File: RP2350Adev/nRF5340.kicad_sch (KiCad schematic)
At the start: 1 part, among them U1 NRF5340-CLAA-R

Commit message: Updated nRF5340 work
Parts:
- removed U1: NRF5340-CLAA-R, WLCSP95_4.390X3.994_NOR, symbol nRF5340:NRF5340-CLAA-R
- added C1, C7, C9: 1.0uF, symbol Device:C
- added C10: 2.2nF, symbol Device:C
- added C11: 2.2uF, symbol Device:C
- added C2, C3: 0.7pF, symbol Device:C
- added C4, C5, C8: 4.7uF, symbol Device:C
- added C6: 100nnF, symbol Device:C
- added L1, L3, L4: 10uH, symbol Device:L
- added L2: 2.2nH, symbol Device:L
- added R1: R, symbol Device:R
- added U1: nRF5340-QKxx, Package_DFN_QFN:Nordic_AQFN-94-1EP_7x7mm_P0.4mm, symbol MCU_Nordic:nRF5340-QKxx
- added X1: 32MHz, symbol Device:Crystal
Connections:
- new net: C10.1, C9.1, L4.2, U1.A27 (DECR), U1.G31 (DECRF)
- new net: C3.1, L2.2, U1.L31 (ANT)
- new net: C2.1, L2.1
- new net: U1.B30 (XC2), X1.1
- new net: U1.C31 (XC1), X1.2
- new net: C7.1, U1.A13 (DECA)
- new net: C1.1, L1.2, U1.A15 (DECD)
- new net: L4.1, U1.A21 (DCC)
- new net: C6.1, U1.A23 (DECN)
- new net: C4.1, R1.2, U1.A5 (VBUS)
- new net: L1.1, U1.B10 (DCCD)
- new net: C5.1, U1.B6 (DECUSB)
- new net: L3.2, U1.J1 (DCCH)
- new net VDD_HV: C8.2, U1.E1 (VDDH)
- new net VDD_nRF: C11.2, L3.1, U1.A19 (VDD), U1.AC1 (VDD), U1.AG1 (VDD), U1.AJ31 (VDD), U1.AL11 (VDD), U1.AL17 (VDD), U1.AL25 (VDD), U1.AL3 (VDD), U1.AL7 (VDD), U1.B28 (VDD), U1.B8 (VDD), U1.C1 (VDD), U1.E31 (VDD), U1.L1 (VDD), U1.N31 (VDD), U1.U1 (VDD)

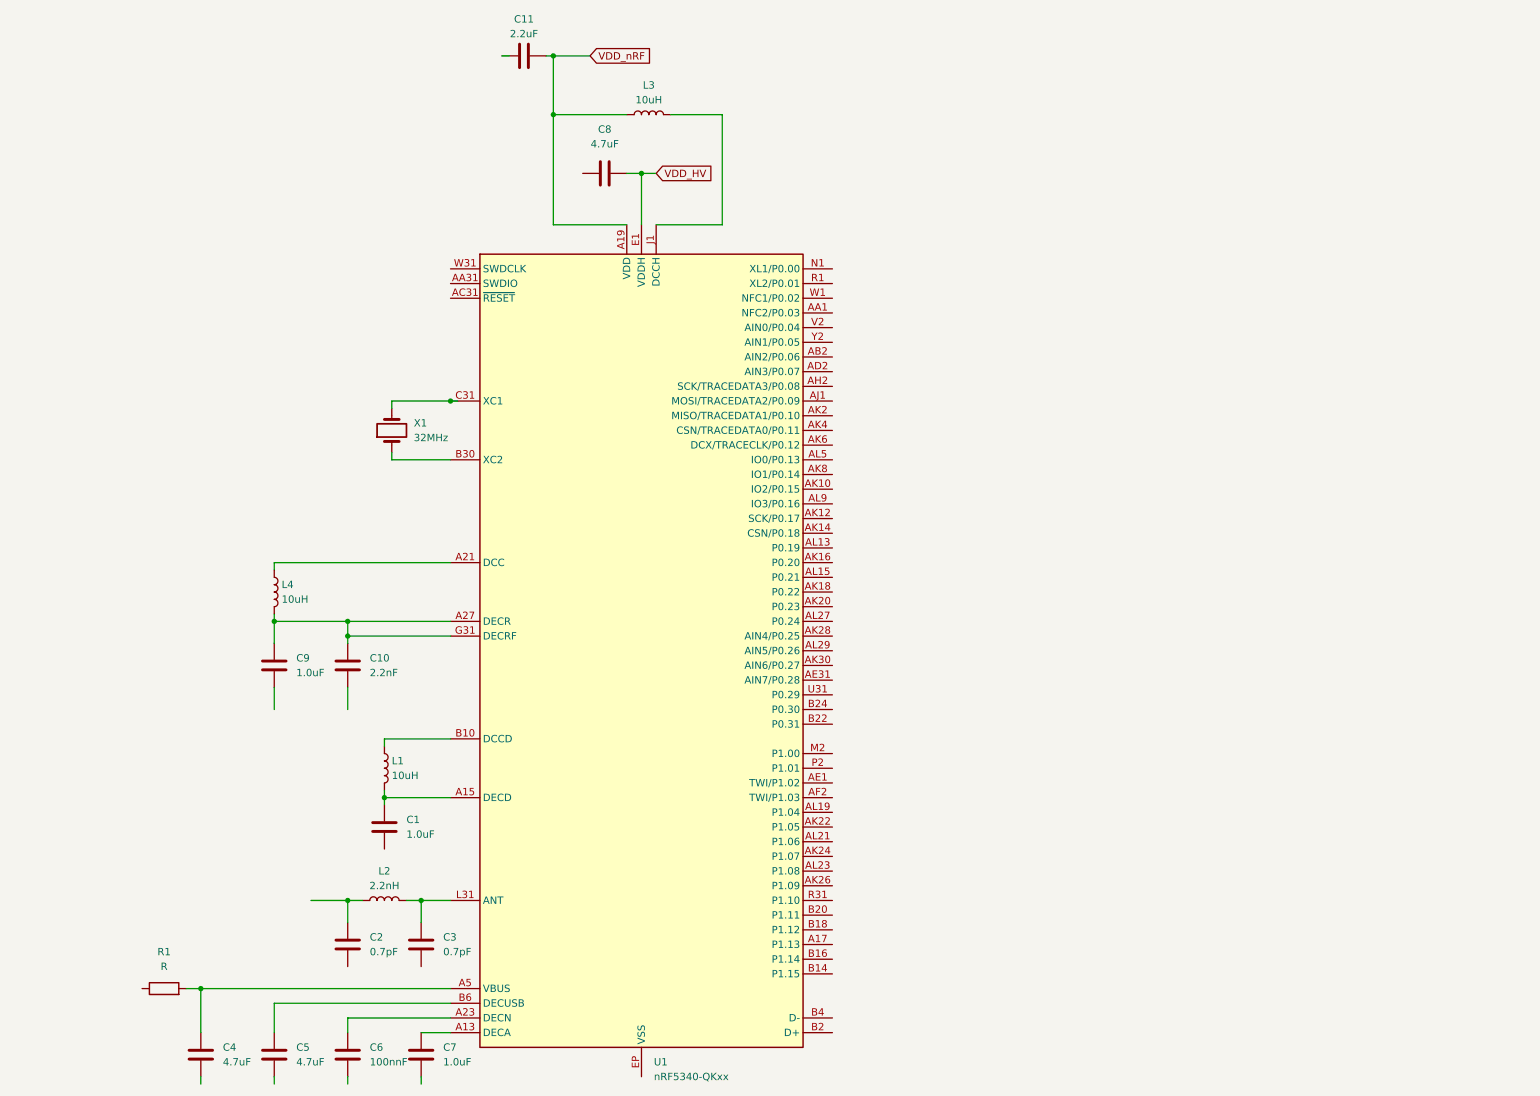
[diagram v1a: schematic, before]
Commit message: Updated nRF5340 schematic
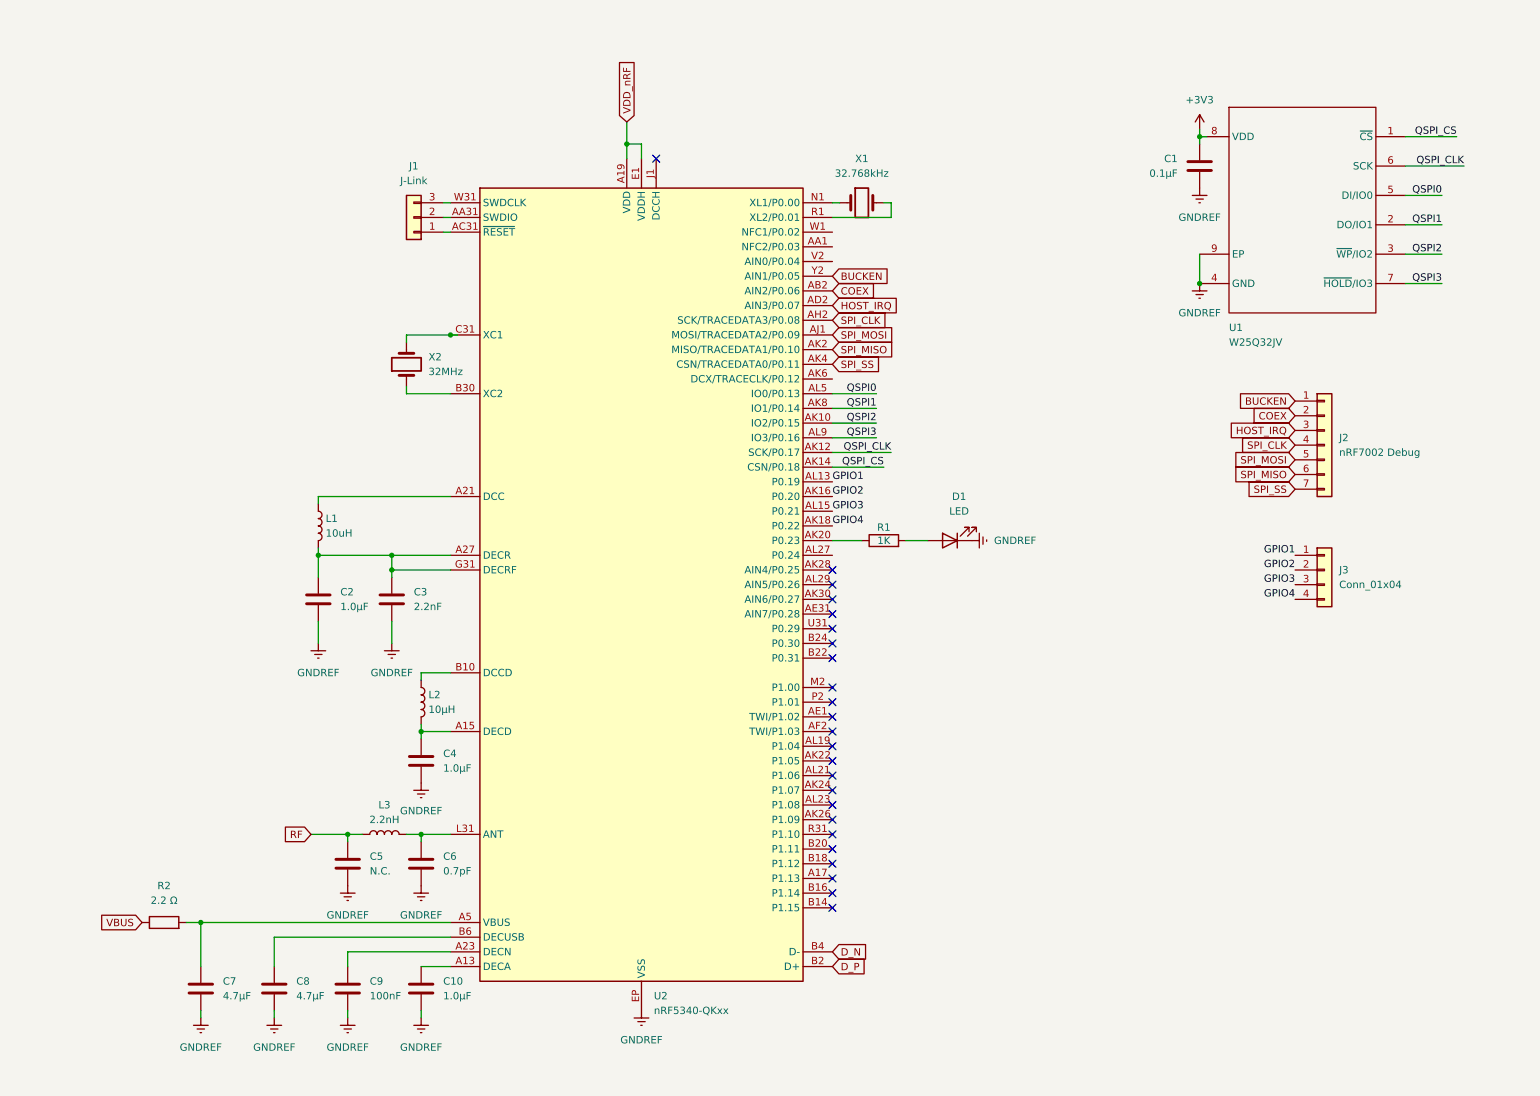
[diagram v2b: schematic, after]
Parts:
- removed C11: 2.2uF, symbol Device:C
- removed C8: 4.7uF, symbol Device:C
- removed L3: 10uH, symbol Device:L
- added C1: 0.1µF, Resistor_SMD:R_0402_1005Metric, symbol Device:C
- added D1: LED, symbol Device:LED
- added J1: J-Link, symbol Connector_Generic:Conn_01x03
- added J2: nRF7002 Debug, symbol Connector_Generic:Conn_01x07
- added J3: Conn_01x04, symbol Connector_Generic:Conn_01x04
- added R1: 1K, Resistor_SMD:R_0402_1005Metric, symbol Device:R
- added U1: W25Q32JV, Package_SON:WSON-8-1EP_6x5mm_P1.27mm_EP3.4x4.3mm, symbol Eclectronics:W25Q128JV
- added X1: 32.768kHz, symbol Device:Crystal
- C10: renamed from C7; value 1.0uF -> 1.0µF
- C2: renamed from C9; value 1.0uF -> 1.0µF
- C4: renamed from C1; value 1.0uF -> 1.0µF
- C5: renamed from C2; value 0.7pF -> N.C.
- C7: renamed from C4; value 4.7uF -> 4.7µF
- C8: renamed from C5; value 4.7uF -> 4.7µF
- C9: renamed from C6; value 100nnF -> 100nF
- L2: renamed from L1; value 10uH -> 10µH
- R2: renamed from R1; value R -> 2.2 Ω
- renumbered C10 to C3, C3 to C6, L4 to L1, L2 to L3, U1 to U2, X1 to X2
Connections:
- net VDD_HV is gone; now on net VDD_nRF: U2.E1 (VDDH)
- net GNDREF: now reaches C2.2
- net GNDREF: now also C10.2, C3.2, C4.2, C5.2, C6.2, C7.2, C8.2, C9.2, U2.EP (VSS), C1.1, D1.1 (K), U1.4 (GND), U1.9 (EP)
- net RF: now reaches C5.1, L3.1
- net at U2.AA31 (SWDIO): now also J1.2 (Pin_2)
- net COEX: now reaches U2.AB2 (AIN2/P0.06)
- net COEX: now also J2.2 (Pin_2)
- net at U2.AC31 (~{RESET}): now also J1.1 (Pin_1)
- net HOST_IRQ: now reaches U2.AD2 (AIN3/P0.07)
- net HOST_IRQ: now also J2.3 (Pin_3)
- net SPI_CLK: now reaches U2.AH2 (SCK/TRACEDATA3/P0.08)
- net SPI_CLK: now also J2.4 (Pin_4)
- net SPI_MOSI: now reaches U2.AJ1 (MOSI/TRACEDATA2/P0.09)
- net SPI_MOSI: now also J2.5 (Pin_5)
- net QSPI2: now reaches U2.AK10 (IO2/P0.15)
- net QSPI2: now also U1.3 (~{WP}/IO2)
- net QSPI_CLK: now reaches U2.AK12 (SCK/P0.17)
- net QSPI_CLK: now also U1.6 (SCK)
- net QSPI_CS: now reaches U2.AK14 (CSN/P0.18)
- net QSPI_CS: now also U1.1 (~{CS})
- net GPIO2: now reaches U2.AK16 (P0.20)
- net GPIO2: now also J3.2 (Pin_2)
- net GPIO4: now reaches U2.AK18 (P0.22)
- net GPIO4: now also J3.4 (Pin_4)
- net SPI_MISO: now reaches U2.AK2 (MISO/TRACEDATA1/P0.10)
- net SPI_MISO: now also J2.6 (Pin_6)
- net at U2.AK20 (P0.23): now also R1.1
- net SPI_SS: now reaches U2.AK4 (CSN/TRACEDATA0/P0.11)
- net SPI_SS: now also J2.7 (Pin_7)
- net QSPI1: now reaches U2.AK8 (IO1/P0.14)
- net QSPI1: now also U1.2 (DO/IO1)
- net GPIO1: now reaches U2.AL13 (P0.19)
- net GPIO1: now also J3.1 (Pin_1)
- net GPIO3: now reaches U2.AL15 (P0.21)
- net GPIO3: now also J3.3 (Pin_3)
- net QSPI0: now reaches U2.AL5 (IO0/P0.13)
- net QSPI0: now also U1.5 (DI/IO0)
- net QSPI3: now reaches U2.AL9 (IO3/P0.16)
- net QSPI3: now also U1.7 (~{HOLD}/IO3)
- net D_P: now reaches U2.B2 (D+)
- net D_N: now reaches U2.B4 (D-)
- net at U2.N1 (XL1/P0.00): now also X1.1
- net at U2.R1 (XL2/P0.01): now also X1.2
- net at U2.W31 (SWDCLK): now also J1.3 (Pin_3)
- net BUCKEN: now reaches U2.Y2 (AIN1/P0.05)
- net BUCKEN: now also J2.1 (Pin_1)
- net VBUS: now reaches R2.1
- new net: D1.2 (A), R1.2
- new net +3V3: C1.2, U1.8 (VDD)
- no-connect marks 0 -> 24
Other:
- moved on the sheet: C10, C2, C3, C4, C5, C6, C7, C8, C9, L1, L2, L3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

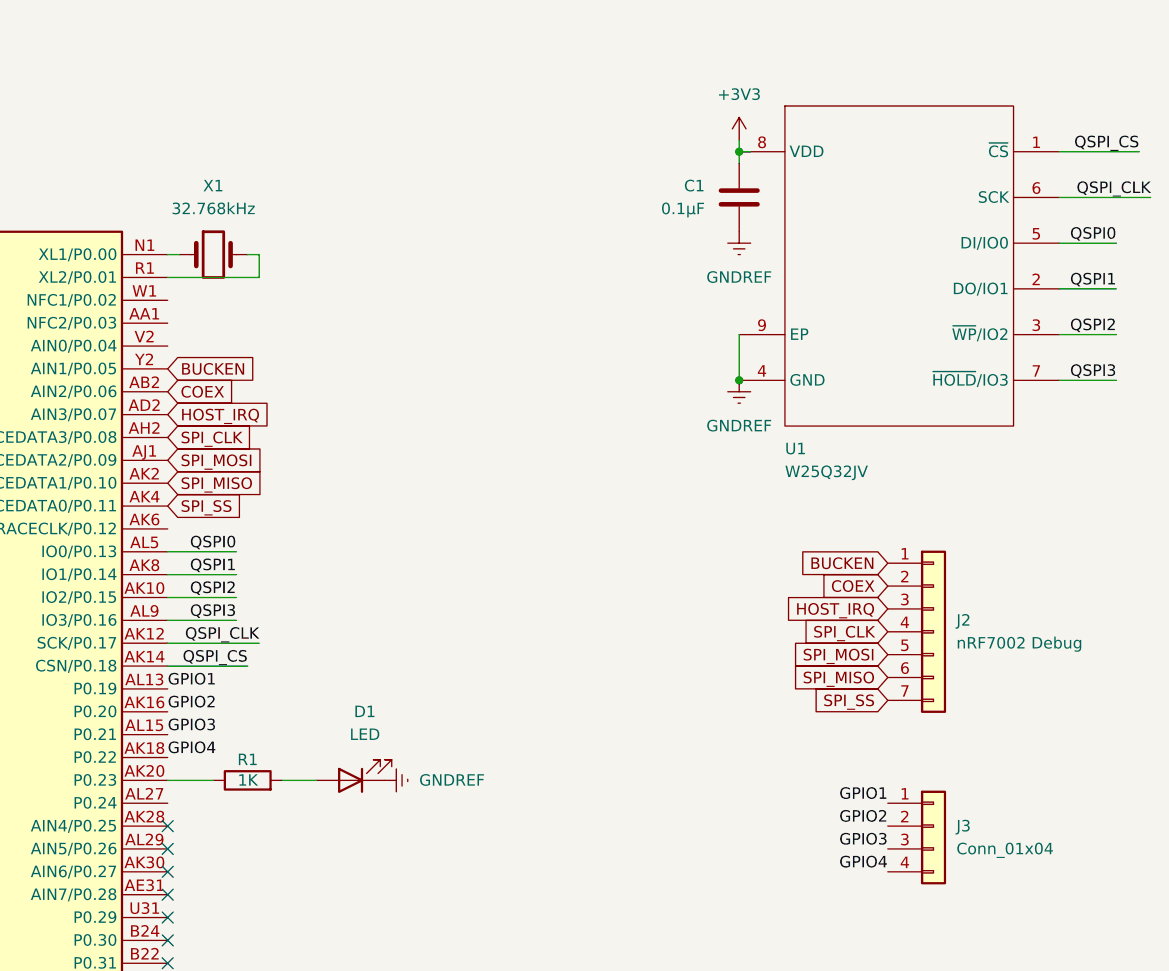
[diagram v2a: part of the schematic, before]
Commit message: link hierarchical sheet and switch from QSPI to SPI
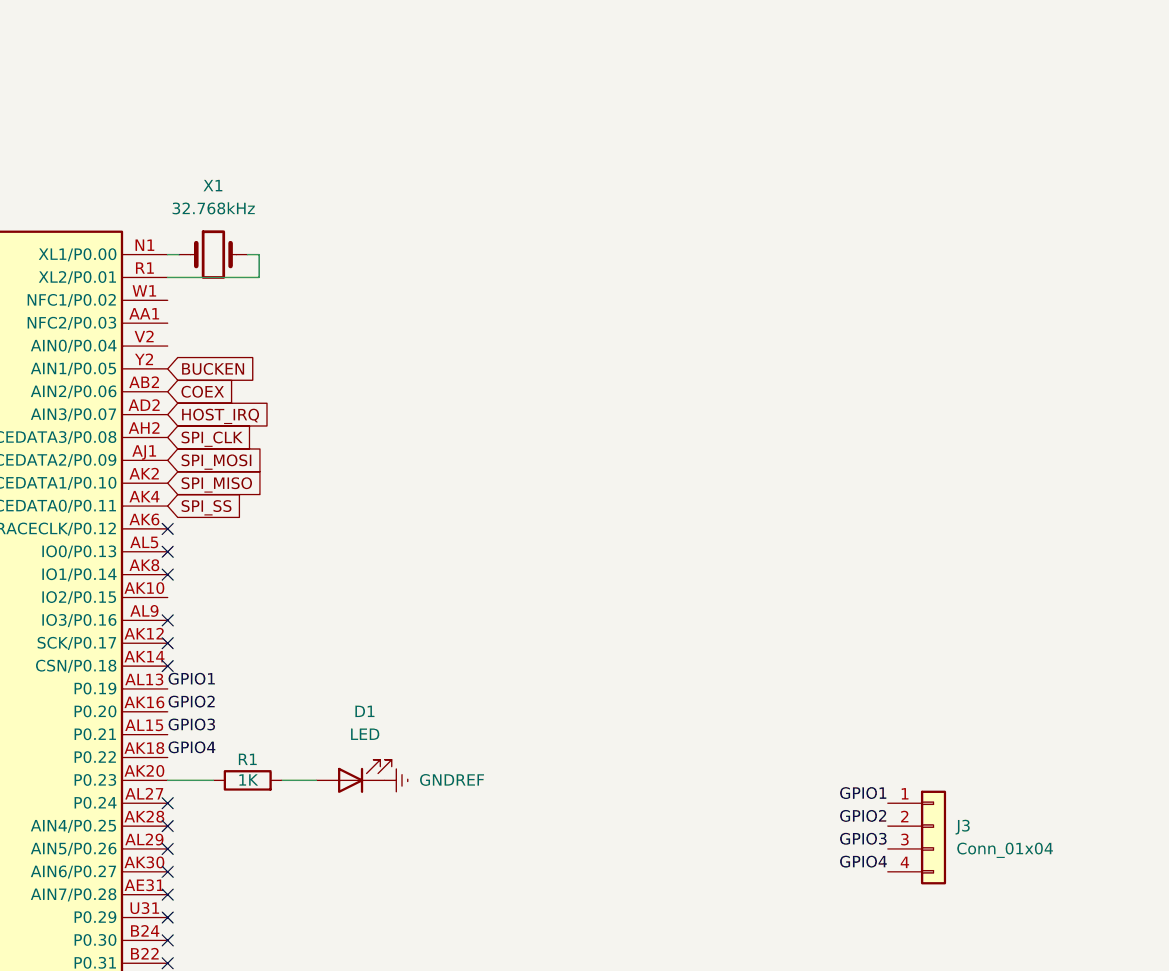
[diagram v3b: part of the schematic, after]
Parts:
- removed C1: 0.1µF, Resistor_SMD:R_0402_1005Metric, symbol Device:C
- removed J2: nRF7002 Debug, symbol Connector_Generic:Conn_01x07
- removed U1: W25Q32JV, Package_SON:WSON-8-1EP_6x5mm_P1.27mm_EP3.4x4.3mm, symbol Eclectronics:W25Q128JV
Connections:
- net QSPI0: no longer names the net of U2.AL5 (IO0/P0.13)
- net QSPI1: no longer names the net of U2.AK8 (IO1/P0.14)
- net QSPI2: no longer names the net of U2.AK10 (IO2/P0.15)
- net QSPI3: no longer names the net of U2.AL9 (IO3/P0.16)
- net QSPI_CLK: no longer names the net of U2.AK12 (SCK/P0.17)
- net QSPI_CS: no longer names the net of U2.AK14 (CSN/P0.18)
- no-connect marks 24 -> 31
